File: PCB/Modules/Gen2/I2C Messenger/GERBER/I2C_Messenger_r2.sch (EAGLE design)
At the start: 25 parts, among them IC1 SN65HVD31DR, IC2 PCA9517, IC3 LM3480-5.0

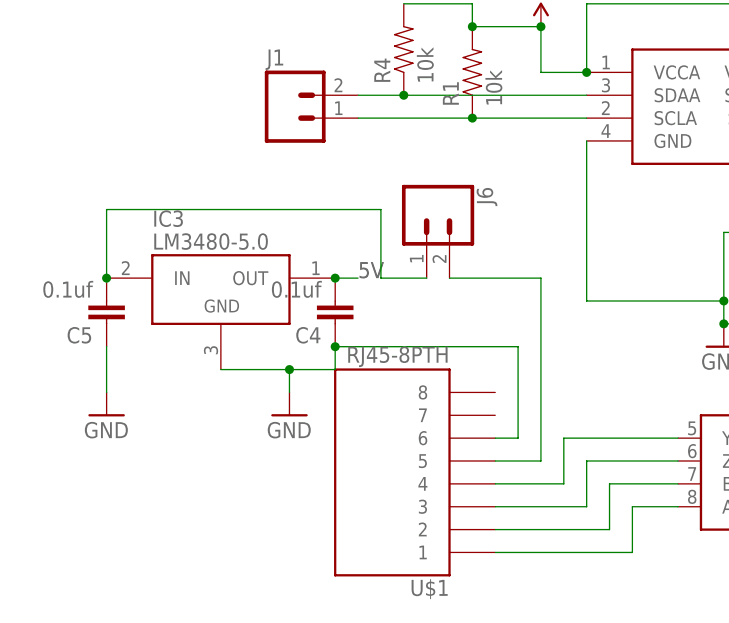
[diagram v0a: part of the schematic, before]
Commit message: -Critical Update for modules with optional RJ45 power (ValveDriver, I2C, SNES and DDS); new PCB designs add a diode to prevent USB power from entering output pin of 5V regulator, when RJ45 (state machine) power is not connected. This update greatly reduces unnecessary power consumption and heat dissipation. If you built a board using the previous designs, please Email a photo of your board to Sanworks support for a free upgrade. -Updated component names on some boards and on web BOMs to avoid skipping parts -Renamed Gen2 module PCB folder from '0.7' to 'Gen2' -Retired pocket state machine (to be replaced with Bpod State Machine r1)
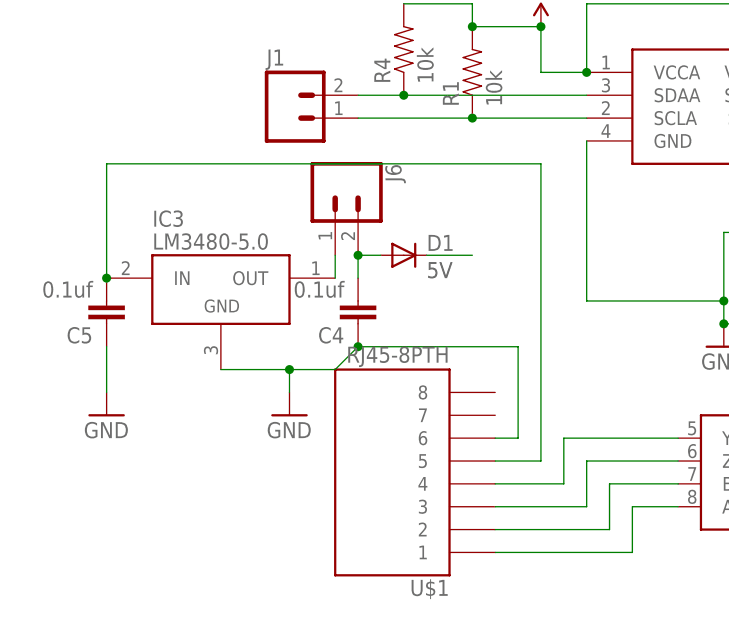
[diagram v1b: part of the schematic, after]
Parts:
- added D1: MBR0520LT, diode:MBR0520LT
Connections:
- new net N$2: IC3.OUT, J6.1
- net 5V: now also D1.C; no longer C4.2, IC3.OUT
- net N$1: now also C4.2, D1.A; no longer U$1.5
- net N$26: now also U$1.5; no longer J6.1
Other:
- moved on the sheet: C4, J6
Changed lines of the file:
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@@
 <part name="GND6" library="SparkFun-Aesthetics" deviceset="GND" device=""/>
 <part name="J6" library="SparkFun-Connectors" deviceset="CONN_02" device=""/>
+<part name="D1" library="diode" deviceset="MBR0520LT" device=""/>
 </parts>
 <sheets>
@@
 <text x="124.46" y="68.58" size="1.778" layer="97">5V</text>
 <text x="119.38" y="99.06" size="1.778" layer="97">5V</text>
-<text x="53.34" y="63.5" size="1.778" layer="97">5V</text>
+<text x="60.96" y="63.5" size="1.778" layer="97">5V</text>
 </plain>
 <instances>
@@
 <instance part="R4" gate="G$1" x="58.42" y="88.9" rot="R90"/>
 <instance part="IC3" gate="G$1" x="38.1" y="63.5"/>
-<instance part="C4" gate="G$1" x="50.8" y="60.96" rot="R180"/>
+<instance part="C4" gate="G$1" x="53.34" y="60.96" rot="R180"/>
 <instance part="C5" gate="G$1" x="25.4" y="60.96" rot="R180"/>
 <instance part="GND2" gate="1" x="25.4" y="48.26"/>
 <instance part="GND6" gate="1" x="45.72" y="48.26"/>
-<instance part="J6" gate="G$1" x="60.96" y="71.12" rot="R270"/>
+<instance part="J6" gate="G$1" x="50.8" y="73.66" rot="R270"/>
+<instance part="D1" gate="G$1" x="58.42" y="66.04" smashed="yes">
+<attribute name="NAME" x="60.96" y="66.5226" size="1.778" layer="95"/>
+</instance>
 </instances>
 <busses>
@@
 <pinref part="C4" gate="G$1" pin="1"/>
 <wire x1="45.72" y1="53.34" x2="50.8" y2="53.34" width="0.1524" layer="91"/>
-<wire x1="50.8" y1="53.34" x2="50.8" y2="55.88" width="0.1524" layer="91"/>
+<wire x1="50.8" y1="53.34" x2="53.34" y2="55.88" width="0.1524" layer="91"/>
 <junction x="45.72" y="53.34"/>
 <pinref part="U$1" gate="G$1" pin="6"/>
 <wire x1="68.58" y1="45.72" x2="71.12" y2="45.72" width="0.1524" layer="91"/>
 <wire x1="71.12" y1="45.72" x2="71.12" y2="55.88" width="0.1524" layer="91"/>
-<wire x1="71.12" y1="55.88" x2="50.8" y2="55.88" width="0.1524" layer="91"/>
-<junction x="50.8" y="55.88"/>
+<wire x1="71.12" y1="55.88" x2="53.34" y2="55.88" width="0.1524" layer="91"/>
+<junction x="53.34" y="55.88"/>
 </segment>
 </net>
@@
 </segment>
 <segment>
-<pinref part="IC3" gate="G$1" pin="OUT"/>
-<wire x1="50.8" y1="63.5" x2="53.34" y2="63.5" width="0.1524" layer="91"/>
-<pinref part="C4" gate="G$1" pin="2"/>
-<junction x="50.8" y="63.5"/>
+<pinref part="D1" gate="G$1" pin="C"/>
+<wire x1="60.96" y1="66.04" x2="66.04" y2="66.04" width="0.1524" layer="91"/>
 </segment>
 </net>
@@
 <segment>
 <pinref part="IC3" gate="G$1" pin="IN"/>
-<wire x1="25.4" y1="71.12" x2="25.4" y2="63.5" width="0.1524" layer="91"/>
+<wire x1="25.4" y1="76.2" x2="25.4" y2="63.5" width="0.1524" layer="91"/>
 <pinref part="C5" gate="G$1" pin="2"/>
 <junction x="25.4" y="63.5"/>
-<wire x1="25.4" y1="71.12" x2="55.88" y2="71.12" width="0.1524" layer="91"/>
-<wire x1="55.88" y1="71.12" x2="55.88" y2="63.5" width="0.1524" layer="91"/>
-<pinref part="J6" gate="G$1" pin="1"/>
-<wire x1="55.88" y1="63.5" x2="60.96" y2="63.5" width="0.1524" layer="91"/>
-</segment>
-</net>
-<net name="N$1" class="0">
-<segment>
+<wire x1="25.4" y1="76.2" x2="73.66" y2="76.2" width="0.1524" layer="91"/>
 <pinref part="U$1" gate="G$1" pin="5"/>
 <wire x1="68.58" y1="43.18" x2="73.66" y2="43.18" width="0.1524" layer="91"/>
-<wire x1="73.66" y1="43.18" x2="73.66" y2="63.5" width="0.1524" layer="91"/>
+<wire x1="73.66" y1="43.18" x2="73.66" y2="76.2" width="0.1524" layer="91"/>
+</segment>
+</net>
+<net name="N$2" class="0">
+<segment>
+<pinref part="J6" gate="G$1" pin="1"/>
+<pinref part="IC3" gate="G$1" pin="OUT"/>
+<wire x1="50.8" y1="66.04" x2="50.8" y2="63.5" width="0.1524" layer="91"/>
+</segment>
+</net>
+<net name="N$1" class="0">
+<segment>
 <pinref part="J6" gate="G$1" pin="2"/>
-<wire x1="73.66" y1="63.5" x2="63.5" y2="63.5" width="0.1524" layer="91"/>
-</segment>
-</net>
+<pinref part="D1" gate="G$1" pin="A"/>
+<wire x1="55.88" y1="66.04" x2="53.34" y2="66.04" width="0.1524" layer="91"/>
+<pinref part="C4" gate="G$1" pin="2"/>
+<wire x1="53.34" y1="66.04" x2="53.34" y2="63.5" width="0.1524" layer="91"/>
+<junction x="53.34" y="66.04"/>
+</segment>
+</net>
